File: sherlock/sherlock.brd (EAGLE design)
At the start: 91.4 x 58.4 mm, 27 parts, among them U3 XBEE-1B2, X1 2540-

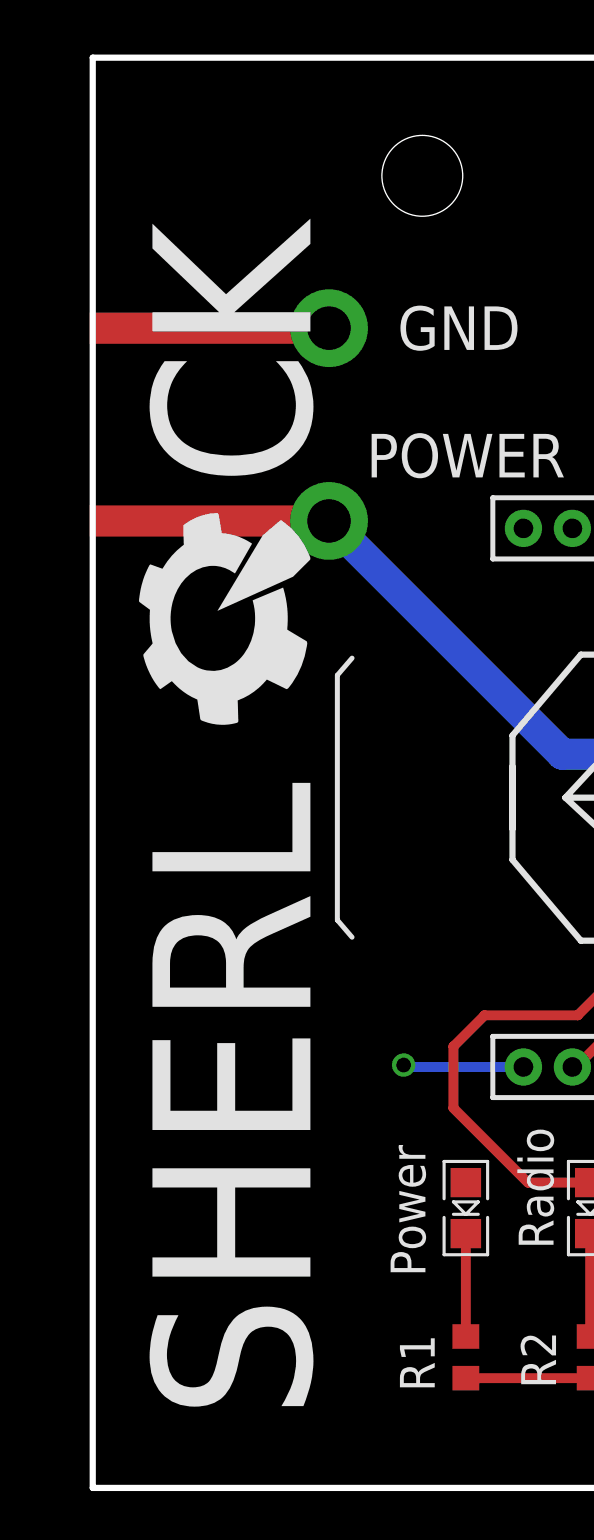
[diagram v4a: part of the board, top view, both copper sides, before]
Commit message: Moved Sherlock name so Anderson pads aren't covered.
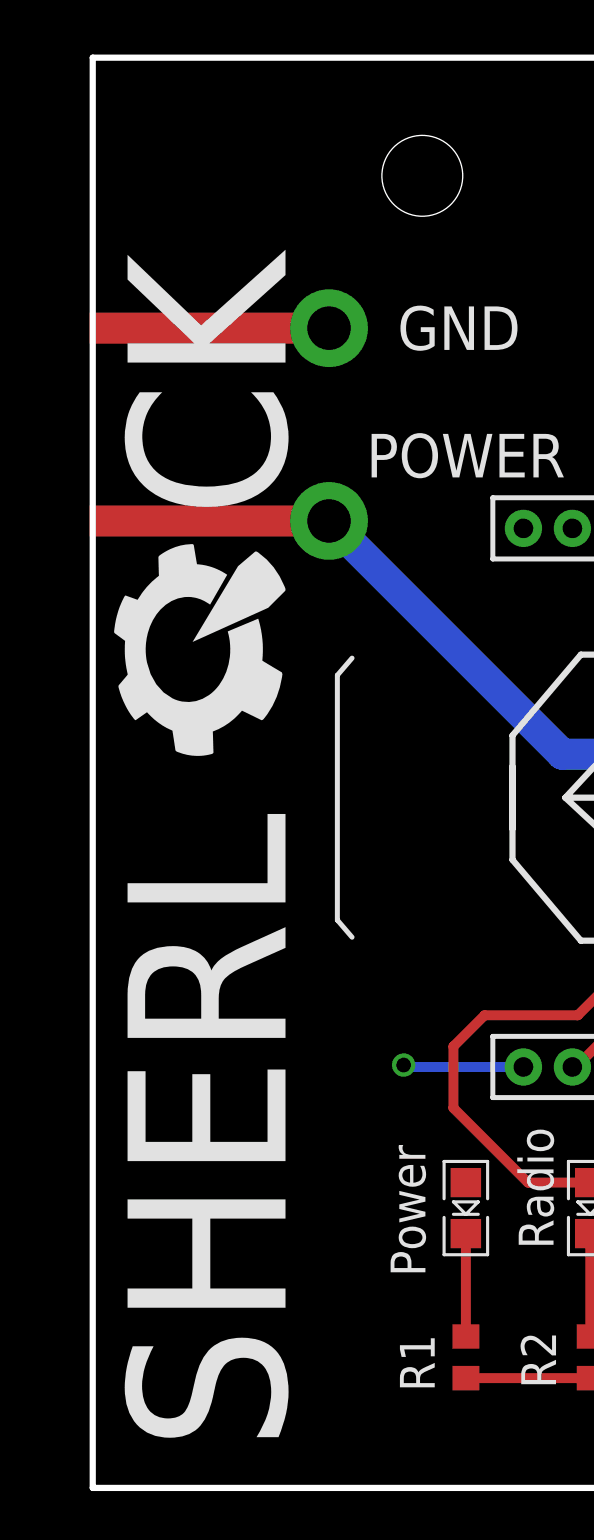
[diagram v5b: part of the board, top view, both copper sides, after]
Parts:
- moved U$2 1.63 mm to (7.87, 1.52)
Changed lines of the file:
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@@
 </element>
 <element name="U$7" library="pie" package="OSHW-LOGO-L" value="" x="60.198" y="28.448" rot="MR0"/>
-<element name="U$2" library="pie" package="SHERLOCK" value="" x="8.89" y="2.794" smashed="yes" rot="R90"/>
+<element name="U$2" library="pie" package="SHERLOCK" value="" x="7.874" y="1.524" smashed="yes" rot="R90"/>
 <element name="POWER" library="pie" package="ANDERSON_HORIZONTAL" value="ANDERSONHORIZONTAL" x="9.652" y="43.434" smashed="yes">
 <attribute name="PARTNUMBER" value="1377G1" x="9.652" y="43.434" size="1.778" layer="27" display="off"/>

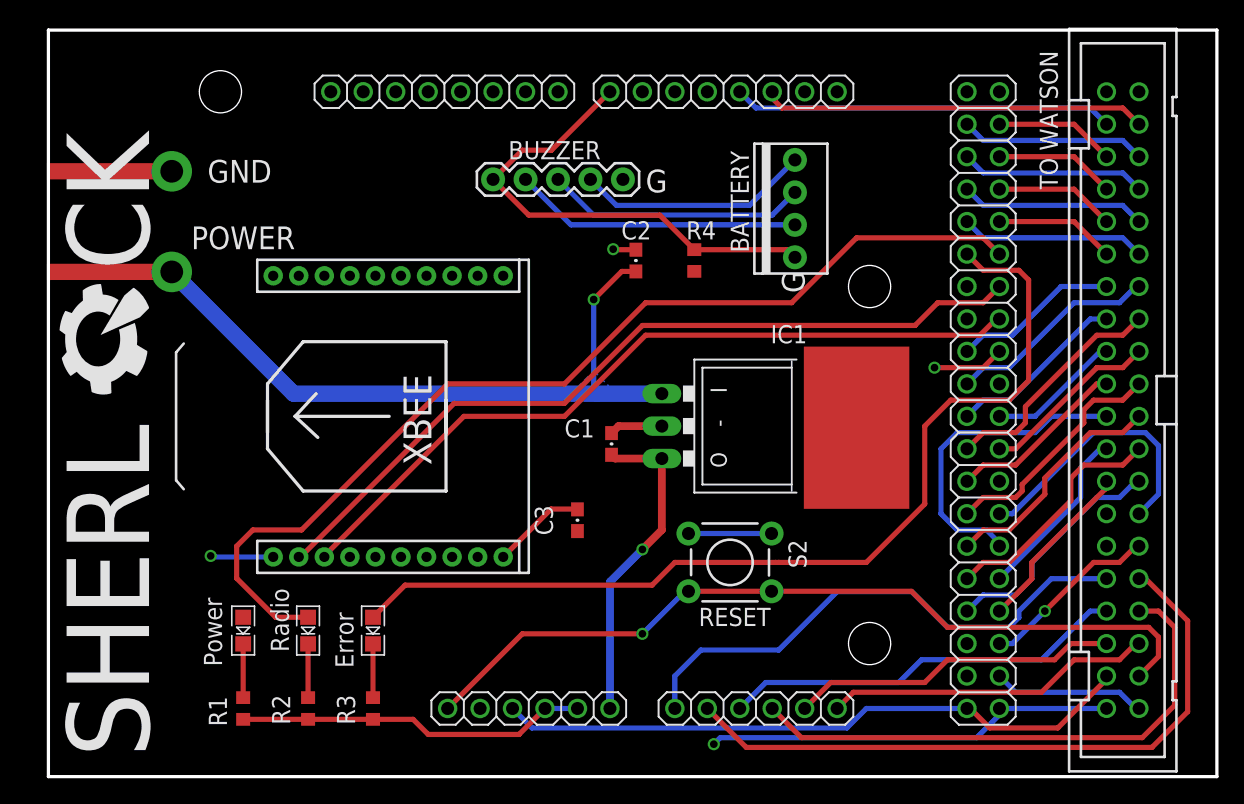
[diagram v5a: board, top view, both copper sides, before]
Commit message: Fixed Sherlock silkscreen
buzzer polarity
moved Panda pin silkscreens to other side, except for the 2 row header,
because there's no easy way to do that one.
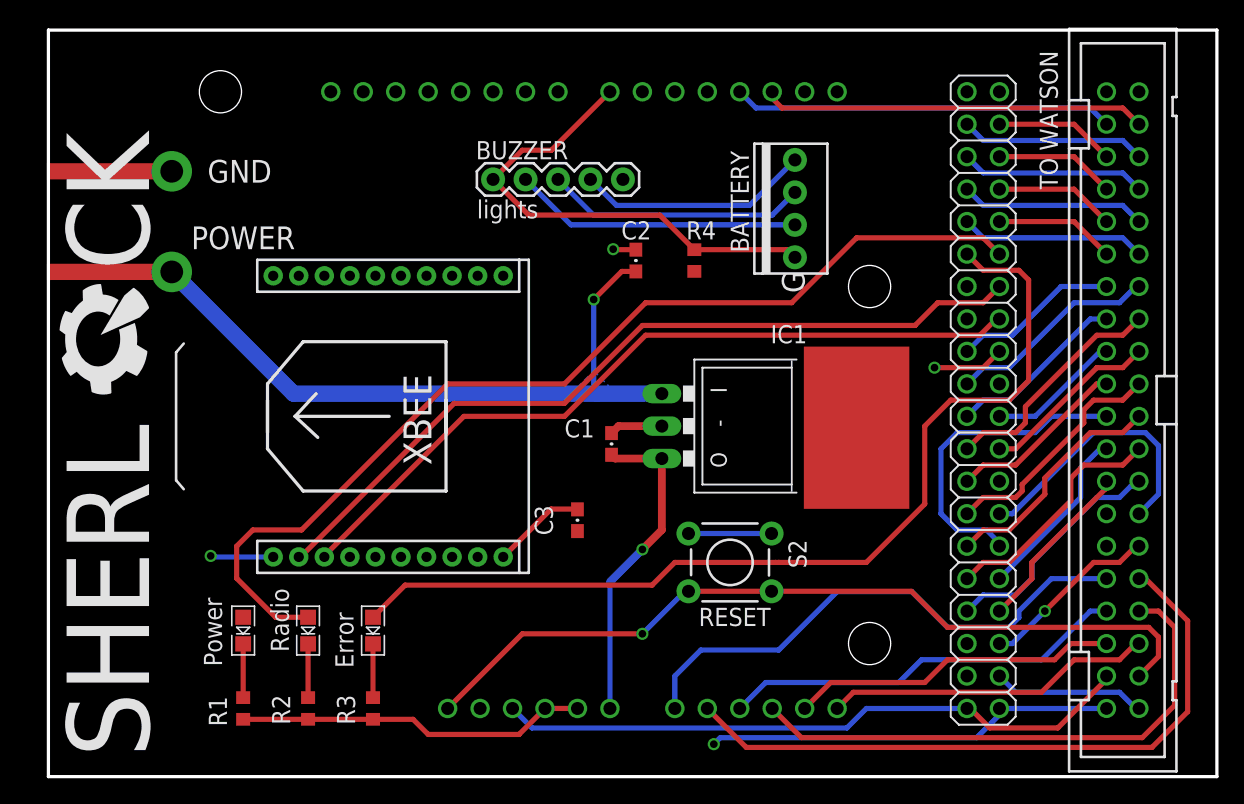
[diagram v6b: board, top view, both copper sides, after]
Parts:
- flipped P1 to the bottom
- flipped P2 to the bottom, turned to 0 degrees
- flipped P4 to the bottom, turned to 180 degrees
- flipped P5 to the bottom, turned to 180 degrees
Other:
- board text added: "TO PANDA"
- board text added: "lights"

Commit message: Further Changes on Sherlock
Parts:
- removed U$2: (no value), pie:SHERLOCK
- added U$1: (no value), pie:PIE-LOGO-SMALL
- renumbered LED1 to POWER_LIGHT, LED2 to RADIO_LIGHT, LED3 to ERROR_LIGHT
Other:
- board text added: "SHERLOCK"
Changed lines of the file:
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@@
 <text x="69.596" y="26.924" size="1.778" layer="22" font="vector" rot="MR270">TO PANDA</text>
 <text x="31.242" y="3.556" size="1.778" layer="22" font="vector" rot="MR180">TO PANDA</text>
+<wire x1="42.418" y1="45.466" x2="42.418" y2="43.688" width="0.254" layer="21"/>
+<wire x1="41.656" y1="44.45" x2="42.418" y2="43.688" width="0.254" layer="21"/>
+<wire x1="42.418" y1="43.688" x2="43.18" y2="44.45" width="0.254" layer="21"/>
+<wire x1="44.196" y1="44.45" x2="44.958" y2="43.688" width="0.254" layer="21"/>
+<wire x1="44.958" y1="43.688" x2="45.72" y2="44.45" width="0.254" layer="21"/>
+<wire x1="44.958" y1="45.466" x2="44.958" y2="43.688" width="0.254" layer="21"/>
+<text x="6.858" y="3.302" size="3.81" layer="21" font="vector" ratio="15" rot="R90">SHERLOCK</text>
 </plain>
 <attributes>
@@
 </element>
 <element name="C2" library="pie" package="0603-CAP" value="10uF" x="45.974" y="40.386" smashed="yes" rot="R90">
-<attribute name="NAME" x="44.831" y="42.037" size="1.4224" layer="25" font="vector" ratio="15"/>
+<attribute name="NAME" x="41.529" y="39.243" size="1.4224" layer="25" font="vector" ratio="15"/>
 <attribute name="VALUE" x="43.815" y="37.338" size="1.397" layer="27" font="vector" ratio="15"/>
 </element>
-<element name="LED1" library="pie" package="LED-0805" value="" x="15.24" y="11.43" smashed="yes" rot="R270">
+<element name="POWER_LIGHT" library="pie" package="LED-0805" value="" x="15.24" y="11.43" smashed="yes" rot="R270">
 <attribute name="VALUE" x="13.335" y="13.97" size="0.4064" layer="25" font="vector" rot="R270"/>
 </element>
-<element name="LED2" library="pie" package="LED-0805" value="" x="20.32" y="11.43" smashed="yes" rot="R270">
+<element name="RADIO_LIGHT" library="pie" package="LED-0805" value="" x="20.32" y="11.43" smashed="yes" rot="R270">
 <attribute name="VALUE" x="18.415" y="13.97" size="0.4064" layer="25" font="vector" rot="R270"/>
 </element>
-<element name="LED3" library="pie" package="LED-0805" value="" x="25.4" y="11.43" smashed="yes" rot="R270">
+<element name="ERROR_LIGHT" library="pie" package="LED-0805" value="" x="25.4" y="11.43" smashed="yes" rot="R270">
 <attribute name="VALUE" x="23.495" y="13.97" size="0.4064" layer="25" font="vector" rot="R270"/>
 </element>
@@
 </element>
 <element name="U$7" library="pie" package="OSHW-LOGO-L" value="" x="60.198" y="28.448" rot="MR0"/>
-<element name="U$2" library="pie" package="SHERLOCK" value="" x="7.874" y="1.524" smashed="yes" rot="R90"/>
 <element name="POWER" library="pie" package="ANDERSON_HORIZONTAL" value="ANDERSONHORIZONTAL" x="9.652" y="43.434" smashed="yes">
 <attribute name="PARTNUMBER" value="1377G1" x="9.652" y="43.434" size="1.778" layer="27" display="off"/>
-<attribute name="NAME" x="11.176" y="41.275" size="1.778" layer="25" font="vector"/>
-</element>
+<attribute name="NAME" x="11.176" y="41.783" size="1.778" layer="25" font="vector"/>
+</element>
+<element name="U$1" library="pie" package="PIE-LOGO-SMALL" value="" x="25.4" y="46.482"/>
 </elements>
 <signals>
@@
 <wire x1="52.07" y1="2.54" x2="52.07" y2="2.794" width="0.4064" layer="1"/>
 <contactref element="R4" pad="1"/>
-<contactref element="LED1" pad="A"/>
+<contactref element="POWER_LIGHT" pad="A"/>
 <polygon width="0.6096" layer="1" isolate="0.2794">
 <vertex x="0" y="0"/>
@@
 <wire x1="19.812" y1="19.304" x2="16.002" y2="19.304" width="0.4064" layer="1"/>
 <wire x1="16.002" y1="19.304" x2="14.732" y2="18.034" width="0.4064" layer="1"/>
-<contactref element="LED2" pad="A"/>
+<contactref element="RADIO_LIGHT" pad="A"/>
 <wire x1="14.732" y1="18.034" x2="14.732" y2="15.5194" width="0.4064" layer="1"/>
 <wire x1="14.732" y1="15.5194" x2="17.78" y2="12.4714" width="0.4064" layer="1"/>
@@
 <wire x1="56.896" y1="16.764" x2="57.15" y2="16.764" width="0.4064" layer="1"/>
 <wire x1="68.58" y1="27.432" x2="70.612" y2="29.464" width="0.4064" layer="1"/>
-<contactref element="LED3" pad="A"/>
+<contactref element="ERROR_LIGHT" pad="A"/>
 <wire x1="68.58" y1="27.432" x2="68.58" y2="21.336" width="0.4064" layer="1"/>
 <wire x1="25.4" y1="12.4714" x2="27.9146" y2="14.986" width="0.4064" layer="1"/>
@@
 <signal name="N$2">
 <contactref element="R1" pad="2"/>
-<contactref element="LED1" pad="C"/>
+<contactref element="POWER_LIGHT" pad="C"/>
 <wire x1="15.24" y1="10.3886" x2="15.24" y2="6.184" width="0.4064" layer="1"/>
 </signal>
 <signal name="N$3">
 <contactref element="R2" pad="2"/>
-<contactref element="LED2" pad="C"/>
+<contactref element="RADIO_LIGHT" pad="C"/>
 <wire x1="20.32" y1="10.3886" x2="20.32" y2="6.184" width="0.4064" layer="1"/>
 </signal>
 <signal name="N$4">
 <contactref element="R3" pad="2"/>
-<contactref element="LED3" pad="C"/>
+<contactref element="ERROR_LIGHT" pad="C"/>
 <wire x1="25.4" y1="10.3886" x2="25.4" y2="6.184" width="0.4064" layer="1"/>
 </signal>
